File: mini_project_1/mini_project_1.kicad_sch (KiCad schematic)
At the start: 14 parts, among them J1 480370001, U2 MCP1700x-330xxTT, U3 MCP6021

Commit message: Create preliminary layout
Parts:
- D1: footprint Diode_SMD:D_0805_2012Metric -> LED_SMD:LED_0805_2012Metric
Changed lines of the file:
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@@
 			)
 		)
-		(property "Footprint" "Diode_SMD:D_0805_2012Metric"
+		(property "Footprint" "LED_SMD:LED_0805_2012Metric"
 			(at 212.09 110.49 0)
 			(effects

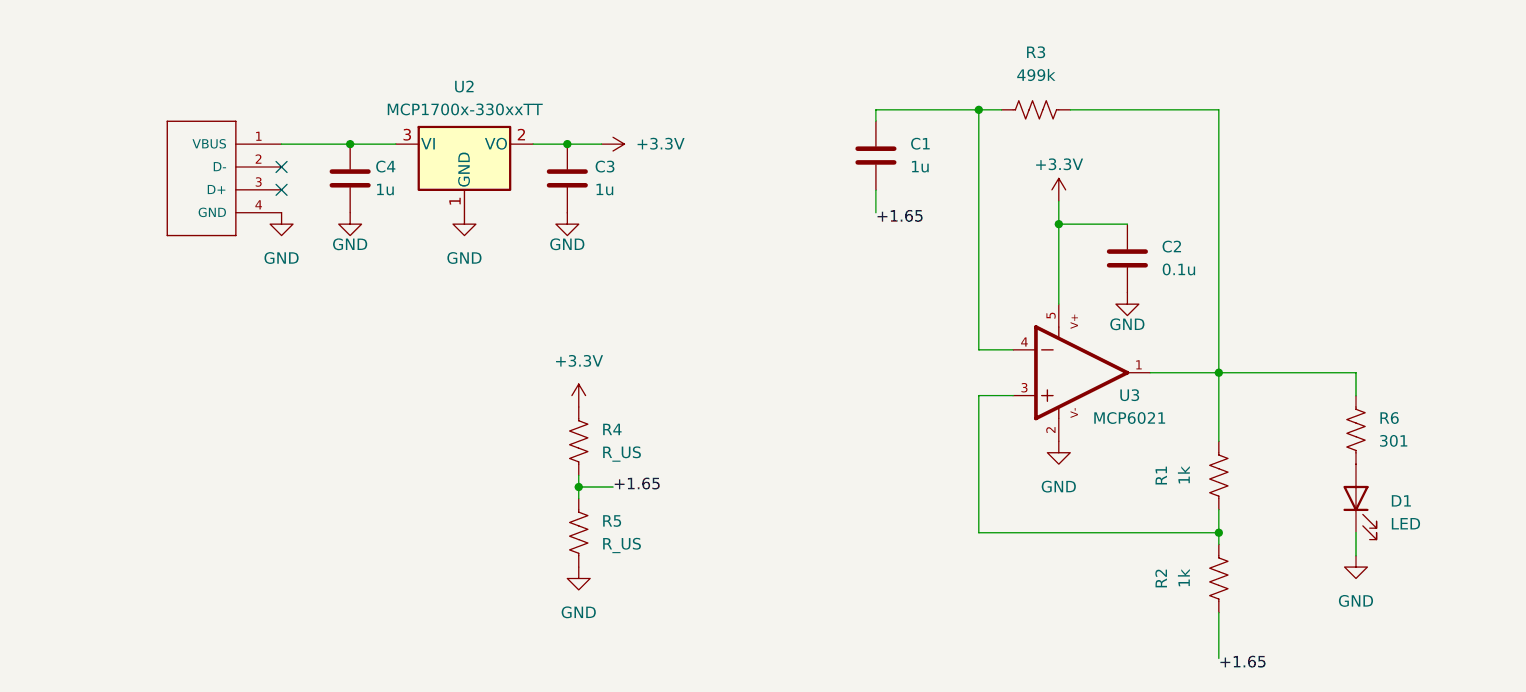
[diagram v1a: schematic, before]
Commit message: Use op amp buffer for 1.65V net
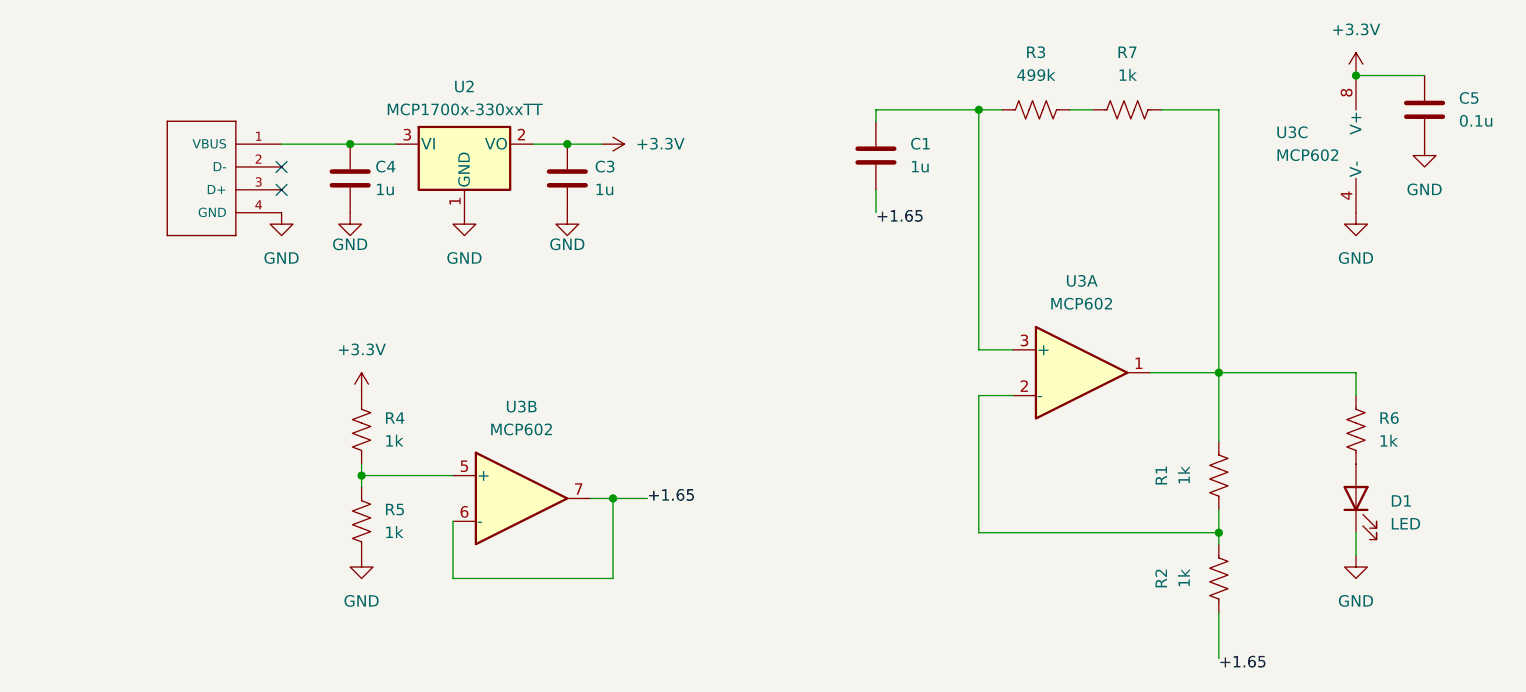
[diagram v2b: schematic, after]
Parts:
- removed C2: 0.1u, Capacitor_SMD:C_0603_1608Metric, symbol Device:C
- removed U3: MCP6021, MCP6021:SOT23-5, symbol MCP6021:MCP6021
- added C5: 0.1u, Capacitor_SMD:C_0603_1608Metric, symbol Device:C
- added R7: 1k, Diode_SMD:D_0603_1608Metric, symbol Device:R_US
- added U3: MCP602, Package_SO:TSSOP-8_4.4x3mm_P0.65mm, symbol Amplifier_Operational:MCP602
- R4, R5: value R_US -> 1k
- R6: value 301 -> 1k
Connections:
- net +1.65: now also U3.6 (-), U3.7; no longer R4.2, R5.1
- net +3.3V: now also C5.1, U3.8 (V+)
- net GND: now also C5.2, U3.4 (V-)
- net at R1.1, R2.2: now also U3.2 (-)
- net at R1.2, R6.1: now also R7.2, U3.1; no longer R3.2
- net at C1.1, R3.1: now also U3.3 (+)
- new net: R4.2, R5.1, U3.5 (+)
- new net: R3.2, R7.1
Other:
- moved on the sheet: R4, R5

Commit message: Modify schematic, layout, and add report
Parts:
- added R5: 499k, Resistor_SMD:R_0603_1608Metric, symbol Device:R_US
- added R6: 49.9k, Resistor_SMD:R_0603_1608Metric, symbol Device:R_US
- C1: value 1u -> 0.1u
- R1, R2: footprint Diode_SMD:D_0603_1608Metric -> Resistor_SMD:R_0603_1608Metric
- R3: value 499k -> 2M; footprint Diode_SMD:D_0603_1608Metric -> Resistor_SMD:R_0603_1608Metric
- R4: renamed from R7; value 1k -> 2M; footprint Diode_SMD:D_0603_1608Metric -> Resistor_SMD:R_0603_1608Metric
- R7: renamed from R4; footprint Diode_SMD:D_0603_1608Metric -> Resistor_SMD:R_0603_1608Metric
- R8: renamed from R5; footprint Diode_SMD:D_0603_1608Metric -> Resistor_SMD:R_0603_1608Metric
- R9: renamed from R6; footprint Diode_SMD:D_0603_1608Metric -> Resistor_SMD:R_0603_1608Metric
- renumbered C4 to C2, C5 to C4, U3 to U1
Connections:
- net at R1.2, R9.1, U1.1: now also R6.2; no longer R4.2
- new net: R4.2, R5.1
- new net: R5.2, R6.1
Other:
- moved on the sheet: C1, C2, C3, C4, D1, R1, R2, R3, R4, R7, R8, R9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
